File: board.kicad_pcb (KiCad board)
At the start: 2 copper layers, 81.3 x 43.2 mm, 14 parts, among them J1 B2B-PH-K-S_LF__SN_, J2 B2B-PH-K-S_LF__SN_, J3 B2B-PH-K-S_LF__SN_, J4 B2B-PH-K-S_LF__SN_, J5 B2B-PH-K-S_LF__SN_, J6 B2B-PH-K-S_LF__SN_, J7 Conn_01x02, J8 B7B-XH-A_LF__SN_

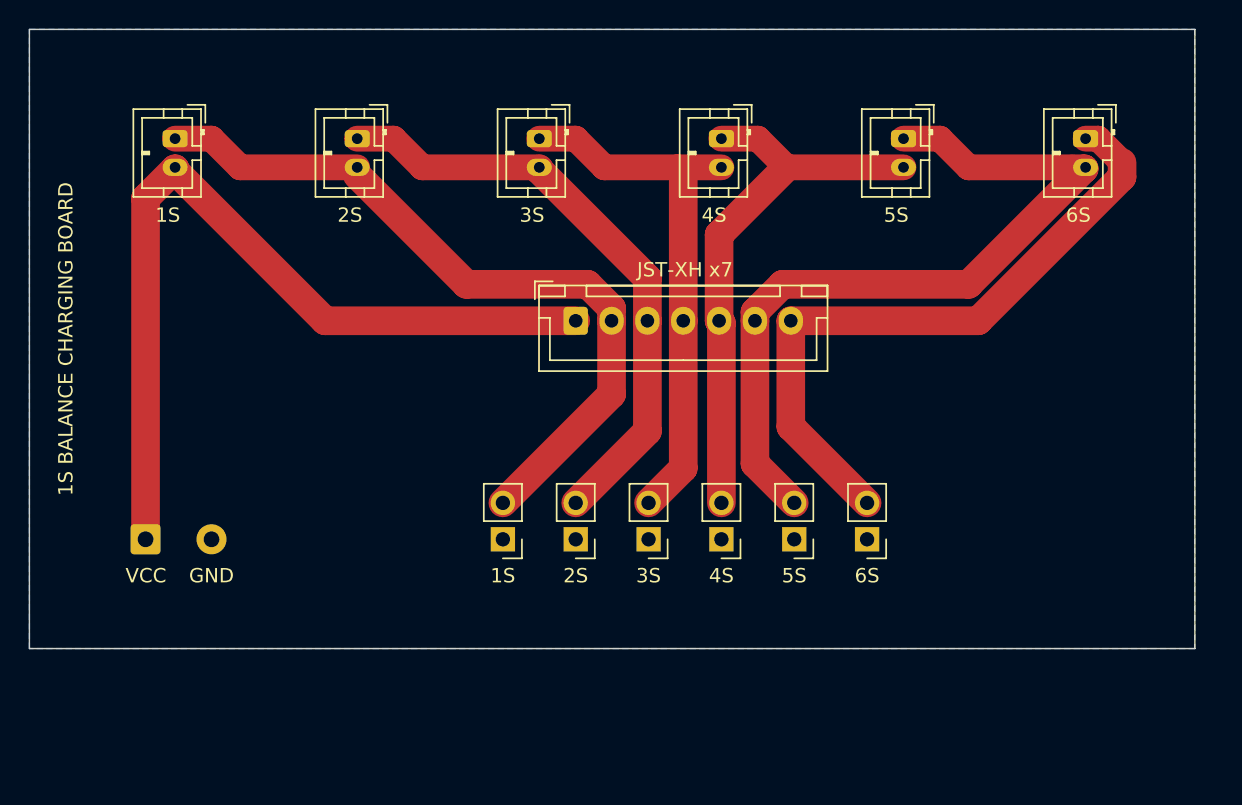
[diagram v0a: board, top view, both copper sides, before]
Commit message: New 1s, 2s and 3s design.
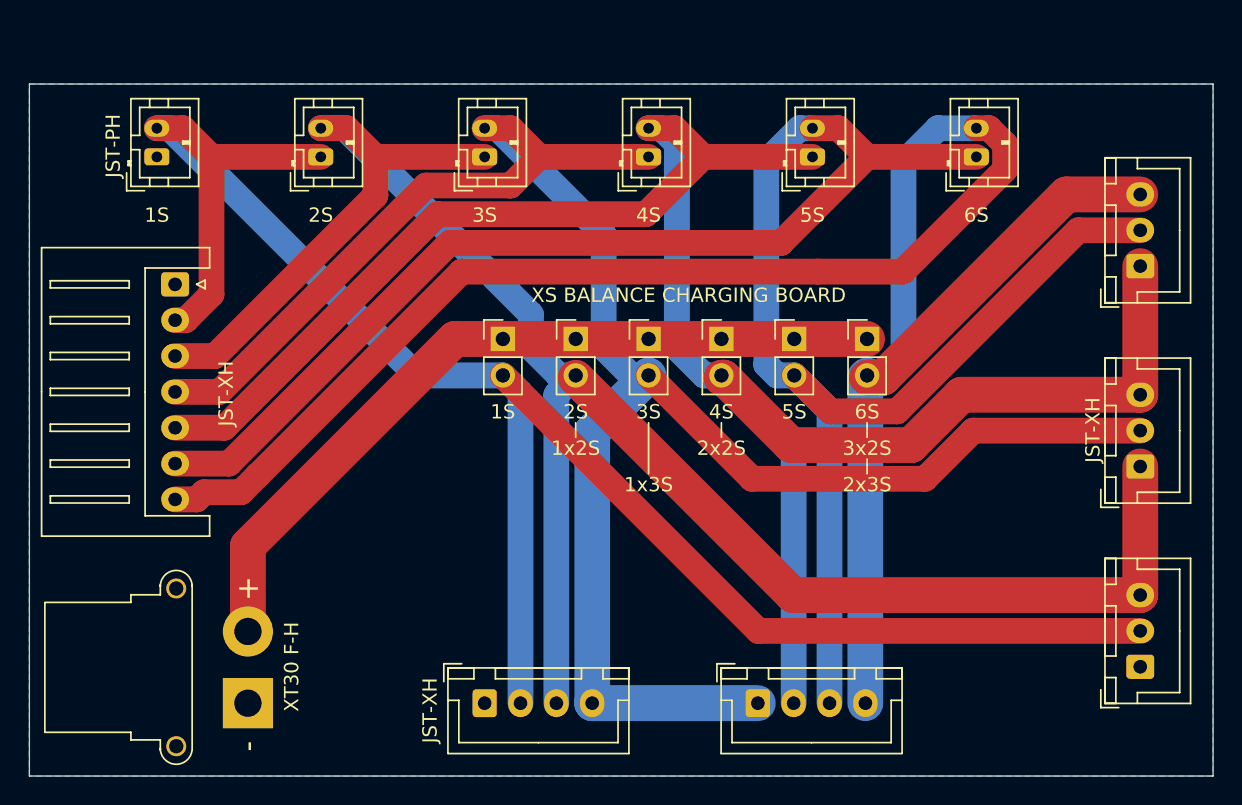
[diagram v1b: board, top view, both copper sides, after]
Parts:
- added J10: Conn_01x04, Connector_JST:JST_XH_B4B-XH-A_1x04_P2.50mm_Vertical, F.Cu at (97.8, 156.2)
- added J11: Conn_01x04, Connector_JST:JST_XH_B4B-XH-A_1x04_P2.50mm_Vertical, F.Cu at (116.8, 156.2)
- added J13: Conn_01x07, Connector_JST:JST_XH_S7B-XH-A_1x07_P2.50mm_Horizontal, F.Cu at (76.2, 127.0)
- added J7: Conn_01x03, Connector_JST:JST_XH_B3B-XH-A_1x03_P2.50mm_Vertical, F.Cu at (143.5, 153.7)
- added J9: Conn_01x03, Connector_JST:JST_XH_B3B-XH-A_1x03_P2.50mm_Vertical, F.Cu at (143.5, 125.7)
- J1, J2, J3, J4, J5, J6: value B2B-PH-K-S_LF__SN_ -> Conn_01x02
- J12: renamed from J7; footprint Connector_Wire:SolderWire-0.5sqmm_1x02_P4.6mm_D0.9mm_OD2.1mm -> Connector_AMASS:AMASS_XT30PW-F_1x02_P2.50mm_Horizontal
- J8: value B7B-XH-A_LF__SN_ -> Conn_01x03; footprint Connector_JST:JST_XH_B7B-XH-A_1x07_P2.50mm_Vertical -> Connector_JST:JST_XH_B3B-XH-A_1x03_P2.50mm_Vertical
- moved J8 40.7 mm to (143.5, 139.7), turned to 90 degrees
- moved JP1 14.0 mm to (99.1, 130.8), turned to 0 degrees
- moved JP2 14.0 mm to (104.1, 130.8), turned to 0 degrees
- moved JP3 14.0 mm to (109.2, 130.8), turned to 0 degrees
- moved JP4 14.0 mm to (114.3, 130.8), turned to 0 degrees
- moved JP5 14.0 mm to (119.4, 130.8), turned to 0 degrees
- moved JP6 14.0 mm to (124.5, 130.8), turned to 0 degrees
- moved J12 13.5 mm to (81.3, 156.2), turned to 90 degrees
- moved J6 7.73 mm to (132.1, 118.1), turned to 90 degrees
- moved J5 6.48 mm to (120.7, 118.1), turned to 90 degrees
- moved J4 5.24 mm to (109.2, 118.1), turned to 90 degrees
- moved J3 4.02 mm to (97.8, 118.1), turned to 90 degrees
- moved J2 2.84 mm to (86.4, 118.1), turned to 90 degrees
- moved J1 1.80 mm to (74.9, 118.1), turned to 90 degrees
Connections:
- J1 pad 1: Net-(J1-Pad1) -> GND
- J1 pad 2: VCC -> Net-(J1-Pad2)
- J12 pad 1: VCC -> GND
- J12 pad 2: GND -> VCC
- J2 pad 1: Net-(J2-Pad1) -> Net-(J1-Pad2)
- J2 pad 2: Net-(J1-Pad1) -> Net-(J10-Pad3)
- J3 pad 1: Net-(J3-Pad1) -> Net-(J10-Pad3)
- J3 pad 2: Net-(J2-Pad1) -> Net-(J10-Pad4)
- J4 pad 1: Net-(J4-Pad1) -> Net-(J10-Pad4)
- J4 pad 2: Net-(J3-Pad1) -> Net-(J11-Pad2)
- J5 pad 1: Net-(J5-Pad1) -> Net-(J11-Pad2)
- J5 pad 2: Net-(J4-Pad1) -> Net-(J11-Pad3)
- J6 pad 1: Net-(J6-Pad1) -> Net-(J11-Pad3)
- J6 pad 2: Net-(J5-Pad1) -> Net-(J11-Pad4)
- J8 pad 1: VCC -> Net-(J10-Pad3)
- J8 pad 2: Net-(J1-Pad1) -> Net-(J10-Pad4)
- J8 pad 3: Net-(J2-Pad1) -> Net-(J11-Pad2)
- JP1 pad 1: GND -> VCC
- JP1 pad 2: Net-(J1-Pad1) -> Net-(J1-Pad2)
- JP2 pad 1: GND -> VCC
- JP2 pad 2: Net-(J2-Pad1) -> Net-(J10-Pad3)
- JP3 pad 1: GND -> VCC
- JP3 pad 2: Net-(J3-Pad1) -> Net-(J10-Pad4)
- JP4 pad 1: GND -> VCC
- JP4 pad 2: Net-(J4-Pad1) -> Net-(J11-Pad2)
- JP5 pad 1: GND -> VCC
- JP5 pad 2: Net-(J5-Pad1) -> Net-(J11-Pad3)
- JP6 pad 1: GND -> VCC
- JP6 pad 2: Net-(J6-Pad1) -> Net-(J11-Pad4)
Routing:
- net Net-(J11-Pad3): track 0.00 -> 144.3 mm
- net Net-(J11-Pad2): track 0.00 -> 144.0 mm
- net Net-(J10-Pad4): track 0.00 -> 142.4 mm
- net Net-(J11-Pad4): track 0.00 -> 141.6 mm
- net Net-(J10-Pad3): track 0.00 -> 137.9 mm
- net Net-(J1-Pad2): track 0.00 -> 131.6 mm
- net Net-(J5-Pad1): track 54.9 -> 0.00 mm
- net Net-(J1-Pad1): track 51.8 -> 0.00 mm
- net Net-(J6-Pad1): track 46.6 -> 0.00 mm
- net Net-(J2-Pad1): track 42.0 -> 0.00 mm
- net Net-(J4-Pad1): track 38.9 -> 0.00 mm
- net Net-(J3-Pad1): track 37.5 -> 0.00 mm
- net VCC: track 59.1 -> 55.1 mm
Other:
- board size 81.3 x 43.2 mm -> 82.5 x 48.3 mm
- board text added: "1x2S"
- board text added: "1x3S"
- board text added: "2x2S"
- board text added: "2x3S"
- board text added: "3x2S"
- board text added: "JST-PH"
- board text added: "JST-XH"
- board text added: "XS BALANCE CHARGING BOARD"
- board text added: "XT30 F-H"
- board text removed: "1S BALANCE CHARGING BOARD"
- board text removed: "GND"
- board text removed: "JST-XH x7"
- board text removed: "VCC"

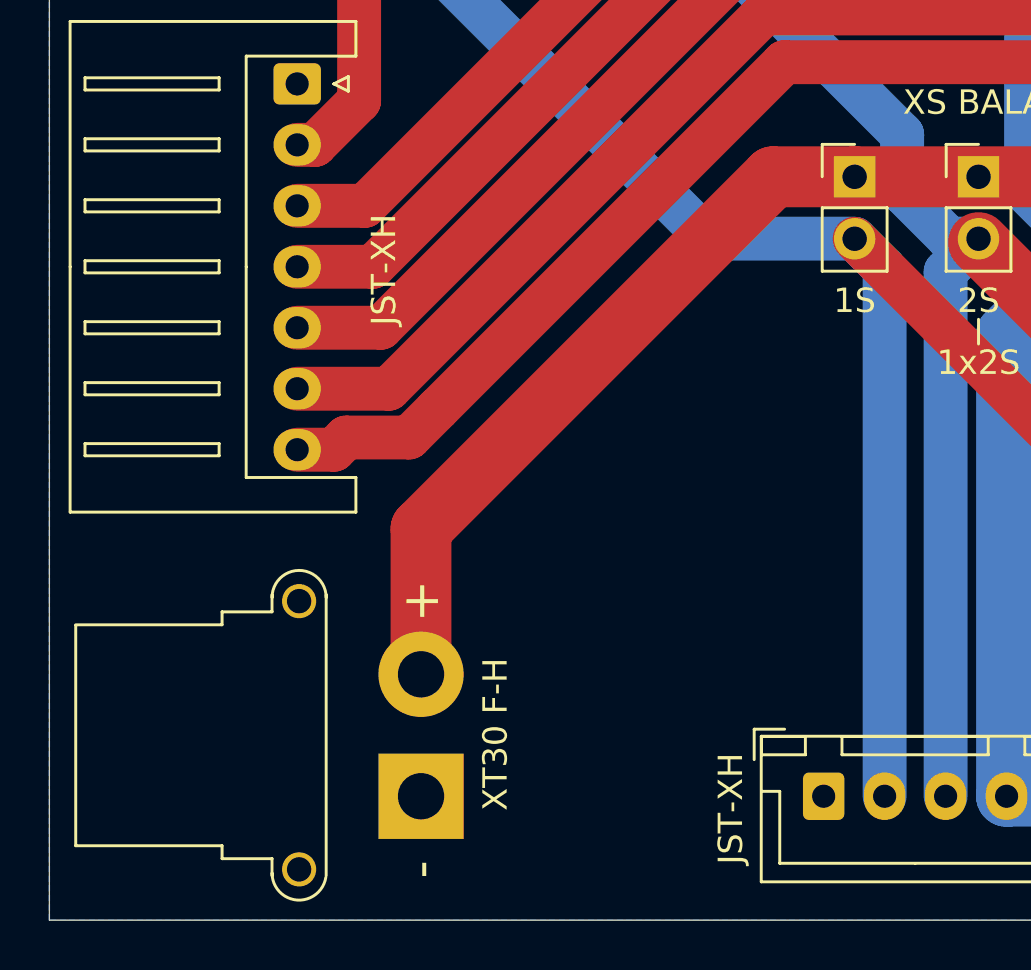
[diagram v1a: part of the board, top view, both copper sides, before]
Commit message: Use correct XT30 connector.
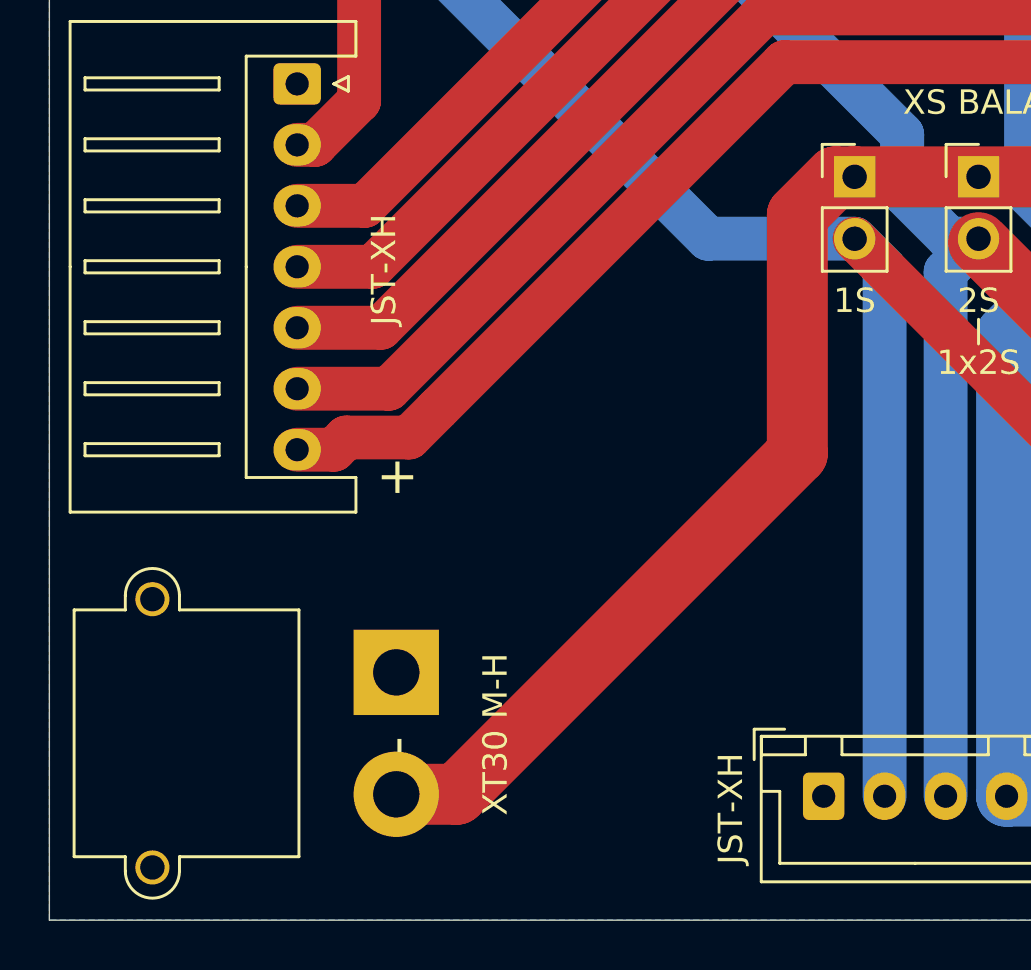
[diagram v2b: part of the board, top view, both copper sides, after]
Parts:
- J12: footprint Connector_AMASS:AMASS_XT30PW-F_1x02_P2.50mm_Horizontal -> Connector_AMASS:AMASS_XT30PW-M_1x02_P2.50mm_Horizontal
- moved J12 5.18 mm to (80.3, 151.1)
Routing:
- net VCC: track 55.1 -> 60.4 mm
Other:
- board text added: "XT30 M-H"
- board text removed: "XT30 F-H"
